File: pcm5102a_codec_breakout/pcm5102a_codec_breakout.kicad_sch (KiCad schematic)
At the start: 17 parts, among them J101 Conn_01x07_Female, J102 AudioJack3, U101 pcm5102a

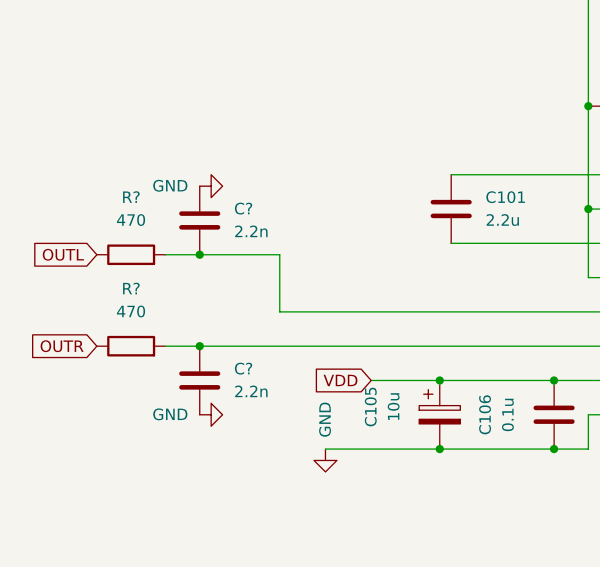
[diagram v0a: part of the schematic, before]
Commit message: [pcm5102a_codec_breakout] Tweaks and fixes
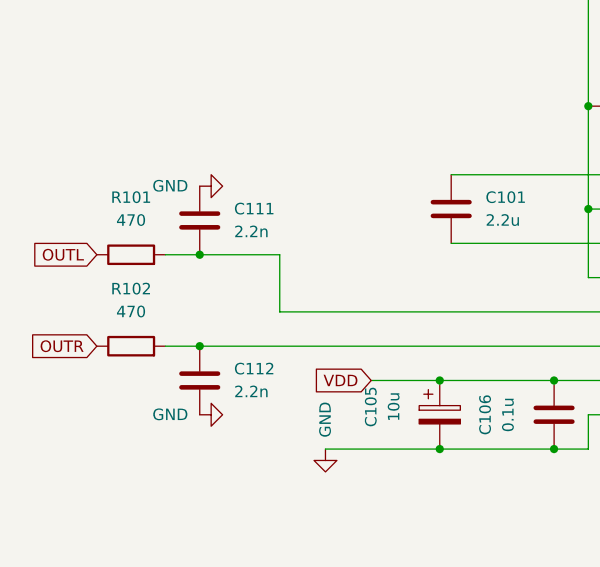
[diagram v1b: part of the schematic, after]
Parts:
- U101: LCSC Part (none) -> C107671
- gave numbers to parts that had none: 4
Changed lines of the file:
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@@
   (symbol (lib_id "Device:R") (at 72.39 105.41 90) (unit 1)
     (in_bom yes) (on_board yes) (fields_autoplaced)
-    (property "Reference" "R?" (id 0) (at 72.39 99.06 90))
+    (property "Reference" "R102" (id 0) (at 72.39 99.06 90))
     (property "Value" "470" (id 1) (at 72.39 101.6 90))
     (property "Footprint" "Resistor_SMD:R_0402_1005Metric" (id 2) (at 72.39 107.188 90)
@@
   (symbol (lib_id "Device:R") (at 72.39 95.25 90) (unit 1)
     (in_bom yes) (on_board yes) (fields_autoplaced)
-    (property "Reference" "R?" (id 0) (at 72.39 88.9 90))
+    (property "Reference" "R101" (id 0) (at 72.39 88.9 90))
     (property "Value" "470" (id 1) (at 72.39 91.44 90))
     (property "Footprint" "Resistor_SMD:R_0402_1005Metric" (id 2) (at 72.39 97.028 90)
@@
   (symbol (lib_id "Device:C") (at 80.01 109.22 180) (unit 1)
     (in_bom yes) (on_board yes) (fields_autoplaced)
-    (property "Reference" "C?" (id 0) (at 83.82 107.9499 0)
+    (property "Reference" "C112" (id 0) (at 83.82 107.9499 0)
       (effects (font (size 1.27 1.27)) (justify right))
     )
@@
   (symbol (lib_id "Device:C") (at 80.01 91.44 180) (unit 1)
     (in_bom yes) (on_board yes) (fields_autoplaced)
-    (property "Reference" "C?" (id 0) (at 83.82 90.1699 0)
+    (property "Reference" "C111" (id 0) (at 83.82 90.1699 0)
       (effects (font (size 1.27 1.27)) (justify right))
     )
@@
     )
     (property "Datasheet" "" (id 3) (at 149.86 101.6 0)
+      (effects (font (size 1.27 1.27)) hide)
+    )
+    (property "LCSC Part" "C107671" (id 4) (at 149.86 101.6 0)
       (effects (font (size 1.27 1.27)) hide)
     )
@@
       (reference "C110") (unit 1) (value "10u") (footprint "Capacitor_SMD:C_Elec_4x5.4")
     )
+    (path "/96785331-65e6-4566-adf9-070f1845b78d"
+      (reference "C111") (unit 1) (value "2.2n") (footprint "Capacitor_SMD:C_0402_1005Metric")
+    )
     (path "/68a9cfb7-b1f7-4eec-b0cd-2984d3a7f61c"
-      (reference "C?") (unit 1) (value "2.2n") (footprint "Capacitor_SMD:C_0402_1005Metric")
-    )
-    (path "/96785331-65e6-4566-adf9-070f1845b78d"
-      (reference "C?") (unit 1) (value "2.2n") (footprint "Capacitor_SMD:C_0402_1005Metric")
+      (reference "C112") (unit 1) (value "2.2n") (footprint "Capacitor_SMD:C_0402_1005Metric")
     )
     (path "/5b65a3c0-d262-4fa1-80ca-93a1a6a2dda9"
@@
       (reference "J102") (unit 1) (value "AudioJack3") (footprint "pcm5102a_codec_breakout:PJ-320B-3A")
     )
+    (path "/66e5ffb0-c929-4d82-8ec0-170327964a62"
+      (reference "R101") (unit 1) (value "470") (footprint "Resistor_SMD:R_0402_1005Metric")
+    )
     (path "/6643bbe7-2449-4b4d-a1a7-c30690faa797"
-      (reference "R?") (unit 1) (value "470") (footprint "Resistor_SMD:R_0402_1005Metric")
-    )
-    (path "/66e5ffb0-c929-4d82-8ec0-170327964a62"
-      (reference "R?") (unit 1) (value "470") (footprint "Resistor_SMD:R_0402_1005Metric")
+      (reference "R102") (unit 1) (value "470") (footprint "Resistor_SMD:R_0402_1005Metric")
     )
     (path "/fcc9186e-ba32-42bb-b54f-c6db5152ae2e"

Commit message: [pcm5102a_codec_breakout] V1 JLCPCB fab files
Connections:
- net OUTL: now also C111.1
- net OUTR: now also C112.2
- net at R102.2, U101.7 (OUTR): no longer C112.2
- net at R101.2, U101.6 (OUTL): no longer C111.1
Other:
- moved on the sheet: C111, C112, R101, R102
